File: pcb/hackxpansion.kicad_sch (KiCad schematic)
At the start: 1 part, among them J2 Conn_02x07_Counter_Clockwise

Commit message: STARTED WORKING ON SYMBOL
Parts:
- removed J2: Conn_02x07_Counter_Clockwise, Connector_PinSocket_2.54mm:PinSocket_2x07_P2.54mm_Horizontal, symbol Connector_Generic:Conn_02x07_Counter_Clockwise
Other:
- added sheet Module Bay 0 (module.kicad_sch)
- added sheet Module Bay 1 (module.kicad_sch)
- added sheet Module Bay 2 (module.kicad_sch)
- added sheet Module Bay 3 (module.kicad_sch)
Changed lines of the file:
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@@
 	(generator_version "10.0")
 	(paper "A4")
-	(symbol
-		(lib_id "Connector_Generic:Conn_02x07_Counter_Clockwise")
-		(at 242.57 87.63 0)
-		(unit 1)
-		(body_style 1)
-		(exclude_from_sim no)
-		(in_bom yes)
-		(on_board yes)
-		(in_pos_files yes)
-		(dnp no)
-		(fields_autoplaced yes)
-		(property "Reference" "J2"
-			(at 243.84 73.66 0)
-			(show_name no)
-			(do_not_autoplace no)
-			(effects
-				(font
-					(size 1.27 1.27)
-				)
-			)
-		)
-		(property "Value" "Conn_02x07_Counter_Clockwise"
-			(at 243.84 76.2 0)
-			(show_name no)
-			(do_not_autoplace no)
-			(effects
-				(font
-					(size 1.27 1.27)
-				)
-			)
-		)
-		(property "Footprint" "Connector_PinSocket_2.54mm:PinSocket_2x07_P2.54mm_Horizontal"
-			(at 242.57 87.63 0)
-			(hide yes)
-			(show_name no)
-			(do_not_autoplace no)
-			(effects
-				(font
-					(size 1.27 1.27)
-				)
-			)
-		)
-		(property "Datasheet" ""
-			(at 242.57 87.63 0)
-			(hide yes)
-			(show_name no)
-			(do_not_autoplace no)
-			(effects
-				(font
-					(size 1.27 1.27)
-				)
-			)
-		)
-		(property "Description" "Generic connector, double row, 02x07, counter clockwise pin numbering scheme (similar to DIP package numbering), script generated (kicad-library-utils/schlib/autogen/connector/)"
-			(at 242.57 87.63 0)
-			(hide yes)
-			(show_name no)
-			(do_not_autoplace no)
-			(effects
-				(font
-					(size 1.27 1.27)
-				)
-			)
-		)
-		(pin "4"
-		)
-		(pin "10"
-		)
-		(pin "1"
-		)
-		(pin "11"
-		)
-		(pin "3"
-		)
-		(pin "2"
-		)
-		(pin "7"
-		)
-		(pin "9"
-		)
-		(pin "12"
-		)
-		(pin "14"
-		)
-		(pin "5"
-		)
-		(pin "13"
-		)
-		(pin "8"
-		)
-		(pin "6"
-		)
-		(instances
-			(project "hackxpansion"
-				(path "/aaf5804d-3f78-442b-969e-39faa388db94"
-					(reference "J2")
-					(unit 1)
-				)
-			)
-		)
-	)
 	(sheet
 		(at 121.92 74.295)
@@
 	)
 	(sheet
-		(at 186.055 111.125)
+		(at 191.135 85.725)
 		(size 12.7 19.05)
 		(exclude_from_sim no)
@@
 		)
 		(property "Sheetname" "Display"
-			(at 186.055 110.4134 0)
+			(at 191.135 85.0134 0)
 			(show_name no)
 			(do_not_autoplace no)
@@
 		)
 		(property "Sheetfile" "disp.kicad_sch"
-			(at 186.055 130.7596 0)
+			(at 191.135 105.3596 0)
 			(show_name no)
 			(do_not_autoplace no)
@@
 				(path "/aaf5804d-3f78-442b-969e-39faa388db94"
 					(page "4")
+				)
+			)
+		)
+	)
+	(sheet
+		(at 232.41 133.35)
+		(size 12.7 11.43)
+		(exclude_from_sim no)
+		(in_bom yes)
+		(on_board yes)
+		(dnp no)
+		(fields_autoplaced yes)
+		(stroke
+			(width 0.1524)
+			(type solid)
+		)
+		(fill
+			(color 0 0 0 0)
+		)
+		(property "Sheetname" "Module Bay 0"
+			(at 232.41 132.6384 0)
+			(show_name no)
+			(do_not_autoplace no)
+			(effects
+				(font
+					(size 1.27 1.27)
+				)
+				(justify left bottom)
+			)
+		)
+		(property "Sheetfile" "module.kicad_sch"
+			(at 232.41 145.3646 0)
+			(show_name no)
+			(do_not_autoplace no)
+			(effects
+				(font
+					(size 1.27 1.27)
+				)
+				(justify left top)
+			)
+		)
+		(instances
+			(project "hackxpansion"
+				(path "/aaf5804d-3f78-442b-969e-39faa388db94"
+					(page "5")
+				)
+			)
+		)
+	)
+	(sheet
+		(at 257.81 133.35)
+		(size 12.7 11.43)
+		(exclude_from_sim no)
+		(in_bom yes)
+		(on_board yes)
+		(dnp no)
+		(fields_autoplaced yes)
+		(stroke
+			(width 0.1524)
+			(type solid)
+		)
+		(fill
+			(color 0 0 0 0)
+		)
+		(property "Sheetname" "Module Bay 1"
+			(at 257.81 132.6384 0)
+			(show_name no)
+			(do_not_autoplace no)
+			(effects
+				(font
+					(size 1.27 1.27)
+				)
+				(justify left bottom)
+			)
+		)
+		(property "Sheetfile" "module.kicad_sch"
+			(at 257.81 145.3646 0)
+			(show_name no)
+			(do_not_autoplace no)
+			(effects
+				(font
+					(size 1.27 1.27)
+				)
+				(justify left top)
+			)
+		)
+		(instances
+			(project "hackxpansion"
+				(path "/aaf5804d-3f78-442b-969e-39faa388db94"
+					(page "6")
+				)
+			)
+		)
+	)
+	(sheet
+		(at 257.81 152.4)
+		(size 12.7 11.43)
+		(exclude_from_sim no)
+		(in_bom yes)
+		(on_board yes)
+		(dnp no)
+		(fields_autoplaced yes)
+		(stroke
+			(width 0.1524)
+			(type solid)
+		)
+		(fill
+			(color 0 0 0 0)
+		)
+		(property "Sheetname" "Module Bay 3"
+			(at 257.81 151.6884 0)
+			(show_name no)
+			(do_not_autoplace no)
+			(effects
+				(font
+					(size 1.27 1.27)
+				)
+				(justify left bottom)
+			)
+		)
+		(property "Sheetfile" "module.kicad_sch"
+			(at 257.81 164.4146 0)
+			(show_name no)
+			(do_not_autoplace no)
+			(effects
+				(font
+					(size 1.27 1.27)
+				)
+				(justify left top)
+			)
+		)
+		(instances
+			(project "hackxpansion"
+				(path "/aaf5804d-3f78-442b-969e-39faa388db94"
+					(page "8")
 				)
 			)
@@
 				)
 			)
+		)
+	)
+	(sheet
+		(at 232.41 152.4)
+		(size 12.7 11.43)
+		(exclude_from_sim no)
+		(in_bom yes)
+		(on_board yes)
+		(dnp no)
+		(fields_autoplaced yes)
+		(stroke
+			(width 0.1524)
+			(type solid)
+		)
+		(fill
+			(color 0 0 0 0)
+		)
+		(property "Sheetname" "Module Bay 2"
+			(at 232.41 151.6884 0)
+			(show_name no)
+			(do_not_autoplace no)
+			(effects
+				(font
+					(size 1.27 1.27)
+				)
+				(justify left bottom)
+			)
+		)
+		(property "Sheetfile" "module.kicad_sch"
+			(at 232.41 164.4146 0)
+			(show_name no)
+			(do_not_autoplace no)
+			(effects
+				(font
+					(size 1.27 1.27)
+				)
+				(justify left top)
+			)
+		)
+		(instances
+			(project "hackxpansion"
+				(path "/aaf5804d-3f78-442b-969e-39faa388db94"
+					(page "7")
+				)
+			)

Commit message: worked on power
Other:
- added sheet Power (pwr.kicad_sch)
- sheet Display ports: added BACKLIGHT, CS, DC, RESET, spi{SPI}; removed none
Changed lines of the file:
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@@
 	)
 	(sheet
-		(at 191.135 85.725)
-		(size 12.7 19.05)
+		(at 197.485 85.725)
+		(size 12.7 15.875)
 		(exclude_from_sim no)
 		(in_bom yes)
@@
 		)
 		(property "Sheetname" "Display"
-			(at 191.135 85.0134 0)
+			(at 197.485 85.0134 0)
 			(show_name no)
 			(do_not_autoplace no)
@@
 		)
 		(property "Sheetfile" "disp.kicad_sch"
-			(at 191.135 105.3596 0)
-			(show_name no)
-			(do_not_autoplace no)
-			(effects
-				(font
-					(size 1.27 1.27)
-				)
-				(justify left top)
+			(at 197.485 102.1846 0)
+			(show_name no)
+			(do_not_autoplace no)
+			(effects
+				(font
+					(size 1.27 1.27)
+				)
+				(justify left top)
+			)
+		)
+		(pin "BACKLIGHT" input
+			(at 197.485 87.63 180)
+			(effects
+				(font
+					(size 1.27 1.27)
+				)
+				(justify left)
+			)
+		)
+		(pin "CS" input
+			(at 197.485 99.06 180)
+			(effects
+				(font
+					(size 1.27 1.27)
+				)
+				(justify left)
+			)
+		)
+		(pin "DC" input
+			(at 197.485 92.71 180)
+			(effects
+				(font
+					(size 1.27 1.27)
+				)
+				(justify left)
+			)
+		)
+		(pin "RESET" input
+			(at 197.485 90.17 180)
+			(effects
+				(font
+					(size 1.27 1.27)
+				)
+				(justify left)
+			)
+		)
+		(pin "spi{SPI}" input
+			(at 197.485 96.52 180)
+			(effects
+				(font
+					(size 1.27 1.27)
+				)
+				(justify left)
 			)
 		)
@@
 				(path "/aaf5804d-3f78-442b-969e-39faa388db94"
 					(page "4")
+				)
+			)
+		)
+	)
+	(sheet
+		(at 193.675 149.86)
+		(size 12.7 3.81)
+		(exclude_from_sim no)
+		(in_bom yes)
+		(on_board yes)
+		(dnp no)
+		(fields_autoplaced yes)
+		(stroke
+			(width 0.1524)
+			(type solid)
+		)
+		(fill
+			(color 0 0 0 0)
+		)
+		(property "Sheetname" "Power"
+			(at 193.675 149.1484 0)
+			(show_name no)
+			(do_not_autoplace no)
+			(effects
+				(font
+					(size 1.27 1.27)
+				)
+				(justify left bottom)
+			)
+		)
+		(property "Sheetfile" "pwr.kicad_sch"
+			(at 193.675 154.2546 0)
+			(show_name no)
+			(do_not_autoplace no)
+			(effects
+				(font
+					(size 1.27 1.27)
+				)
+				(justify left top)
+			)
+		)
+		(instances
+			(project "hackxpansion"
+				(path "/aaf5804d-3f78-442b-969e-39faa388db94"
+					(page "9")
 				)
 			)
@@
 	)
 	(sheet
-		(at 166.37 85.09)
-		(size 16.51 19.05)
+		(at 196.85 111.125)
+		(size 16.51 18.415)
 		(exclude_from_sim no)
 		(in_bom yes)
@@
 		)
 		(property "Sheetname" "ADC"
-			(at 166.37 84.3784 0)
+			(at 196.85 110.4134 0)
 			(show_name no)
 			(do_not_autoplace no)
@@
 		)
 		(property "Sheetfile" "ADC.kicad_sch"
-			(at 166.37 104.7246 0)
+			(at 196.85 130.1246 0)
 			(show_name no)
 			(do_not_autoplace no)
@@
 		)
 		(pin "ALERT" output
-			(at 166.37 87.63 180)
+			(at 196.85 113.03 180)
 			(effects
 				(font
@@
 		)
 		(pin "i2c0{I2C}" bidirectional
-			(at 166.37 90.17 180)
+			(at 196.85 115.57 180)
 			(effects
 				(font
@@
 		)
 		(pin "mod0{DET}" input
-			(at 182.88 93.98 0)
+			(at 213.36 119.38 0)
 			(effects
 				(font
@@
 		)
 		(pin "mod1{DET}" input
-			(at 182.88 96.52 0)
+			(at 213.36 121.92 0)
 			(effects
 				(font
@@
 		)
 		(pin "mod2{DET}" input
-			(at 182.88 99.06 0)
+			(at 213.36 124.46 0)
 			(effects
 				(font
@@
 		)
 		(pin "mod3{DET}" input
-			(at 182.88 101.6 0)
-			(effects
-				(font
+			(at 213.36 127 0)
+			(effects
+				(font

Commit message: worked on power
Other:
- note added: "E24 for the sensing resistors"
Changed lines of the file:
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@@
 	(generator_version "10.0")
 	(paper "A4")
+	(text "E24 for the sensing resistors"
+		(exclude_from_sim no)
+		(at 213.106 75.184 0)
+		(effects
+			(font
+				(size 1.27 1.27)
+			)
+		)
+	)
 	(sheet
 		(at 121.92 74.295)

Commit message: worked on power
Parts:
- added BT1: Battery_Cell, symbol Device:Battery_Cell
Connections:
- new net GND: BT1.2 (-)
- new net Power/+BATT: BT1.1 (+)
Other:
- added sheet USB (usb.kicad_sch)
- sheet Power ports: added +BATT, 3V3, VBUS; removed none
- sheet RP2354B ports: added USB_D+, USB_D-; removed none

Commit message: worked on io banks
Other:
- sheet ADC ports: added {I2C}; removed i2c0{I2C}
- sheet Module Bay 0 ports: added {DET}, {GPIO_BANK}; removed none
- sheet Module Bay 1 ports: added {DET}, {GPIO_BANK}; removed none
- sheet Module Bay 2 ports: added {DET}, {GPIO_BANK}; removed none
- sheet Module Bay 3 ports: added {DET}, {GPIO_BANK}; removed none
- sheet Power ports: added none; removed 3V3
- sheet RP2354B ports: added mod0{GPIO_BANK}, mod1{GPIO_BANK}, mod2{GPIO_BANK}, mod3{GPIO_BANK}, {USB}; removed USB_D+, USB_D-
- sheet USB ports: added VBUS, {USB}; removed none
- note removed: "E24 for the sensing resistors"
- moved on the sheet: BT1

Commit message: did a bunch of gpio bank stuff
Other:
- sheet Display ports: added {SPI}; removed spi{SPI}
- sheet RP2354B ports: added ADC_ALERT, DISP_BACKLIGHT, DISP_CS, DISP_DC, adc{I2C}, disp{SPI}; removed none
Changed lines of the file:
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@@
 	(wire
 		(pts
+			(xy 137.16 74.93) (xy 156.21 74.93)
+		)
+		(stroke
+			(width 0)
+			(type default)
+		)
+	)
+	(wire
+		(pts
+			(xy 137.16 69.85) (xy 156.21 69.85)
+		)
+		(stroke
+			(width 0)
+			(type default)
+		)
+	)
+	(wire
+		(pts
 			(xy 98.425 140.97) (xy 98.425 142.24)
 		)
@@
 		)
 	)
+	(bus
+		(pts
+			(xy 137.16 93.98) (xy 191.77 93.98)
+		)
+		(stroke
+			(width 0)
+			(type default)
+		)
+	)
 	(wire
 		(pts
@@
 		)
 	)
+	(wire
+		(pts
+			(xy 137.16 81.28) (xy 156.21 81.28)
+		)
+		(stroke
+			(width 0)
+			(type default)
+		)
+	)
 	(bus
 		(pts
@@
 	(bus
 		(pts
+			(xy 137.16 78.74) (xy 156.21 78.74)
+		)
+		(stroke
+			(width 0)
+			(type default)
+		)
+	)
+	(bus
+		(pts
 			(xy 92.71 123.19) (xy 92.71 114.3)
 		)
@@
 		(pts
 			(xy 140.97 114.3) (xy 140.97 144.78)
+		)
+		(stroke
+			(width 0)
+			(type default)
+		)
+	)
+	(wire
+		(pts
+			(xy 137.16 91.44) (xy 191.77 91.44)
 		)
 		(stroke
@@
 			)
 		)
+		(pin "ADC_ALERT" input
+			(at 137.16 91.44 0)
+			(effects
+				(font
+					(size 1.27 1.27)
+				)
+				(justify right)
+			)
+		)
+		(pin "adc{I2C}" bidirectional
+			(at 137.16 93.98 0)
+			(effects
+				(font
+					(size 1.27 1.27)
+				)
+				(justify right)
+			)
+		)
+		(pin "DISP_BACKLIGHT" output
+			(at 137.16 69.85 0)
+			(effects
+				(font
+					(size 1.27 1.27)
+				)
+				(justify right)
+			)
+		)
+		(pin "DISP_CS" output
+			(at 137.16 81.28 0)
+			(effects
+				(font
+					(size 1.27 1.27)
+				)
+				(justify right)
+			)
+		)
+		(pin "DISP_DC" output
+			(at 137.16 74.93 0)
+			(effects
+				(font
+					(size 1.27 1.27)
+				)
+				(justify right)
+			)
+		)
+		(pin "disp{SPI}" bidirectional
+			(at 137.16 78.74 0)
+			(effects
+				(font
+					(size 1.27 1.27)
+				)
+				(justify right)
+			)
+		)
 		(instances
 			(project "hackxpansion"
@@
 			)
 		)
-		(pin "spi{SPI}" input
+		(pin "{SPI}" bidirectional
 			(at 156.21 78.74 180)
 			(effects
@@
 		)
 		(pin "ALERT" output
-			(at 191.77 90.805 180)
-			(effects
-				(font
+			(at 191.77 91.44 180)
+			(effects
+				(font

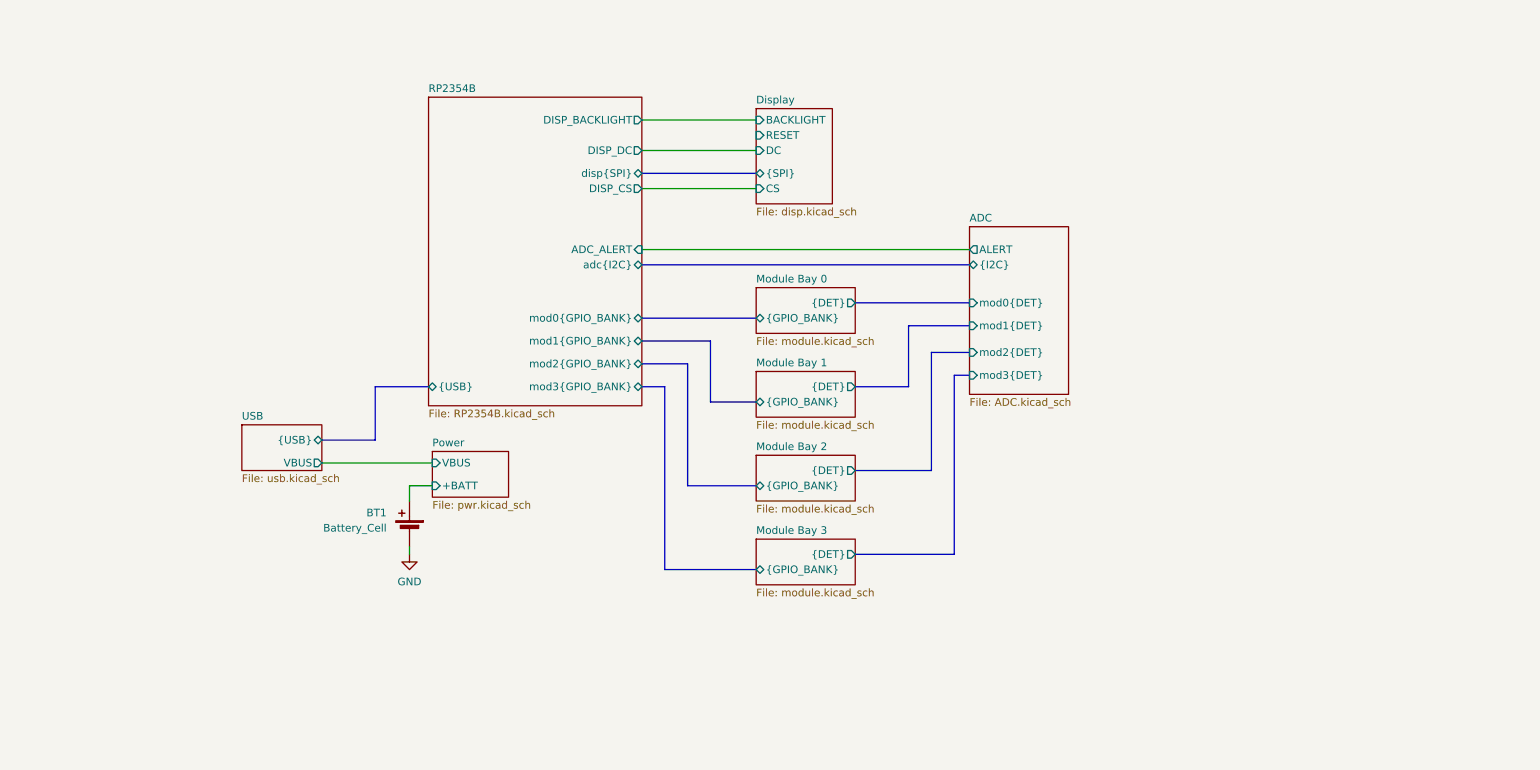
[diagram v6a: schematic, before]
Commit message: started to split up the schematic into two pcbs
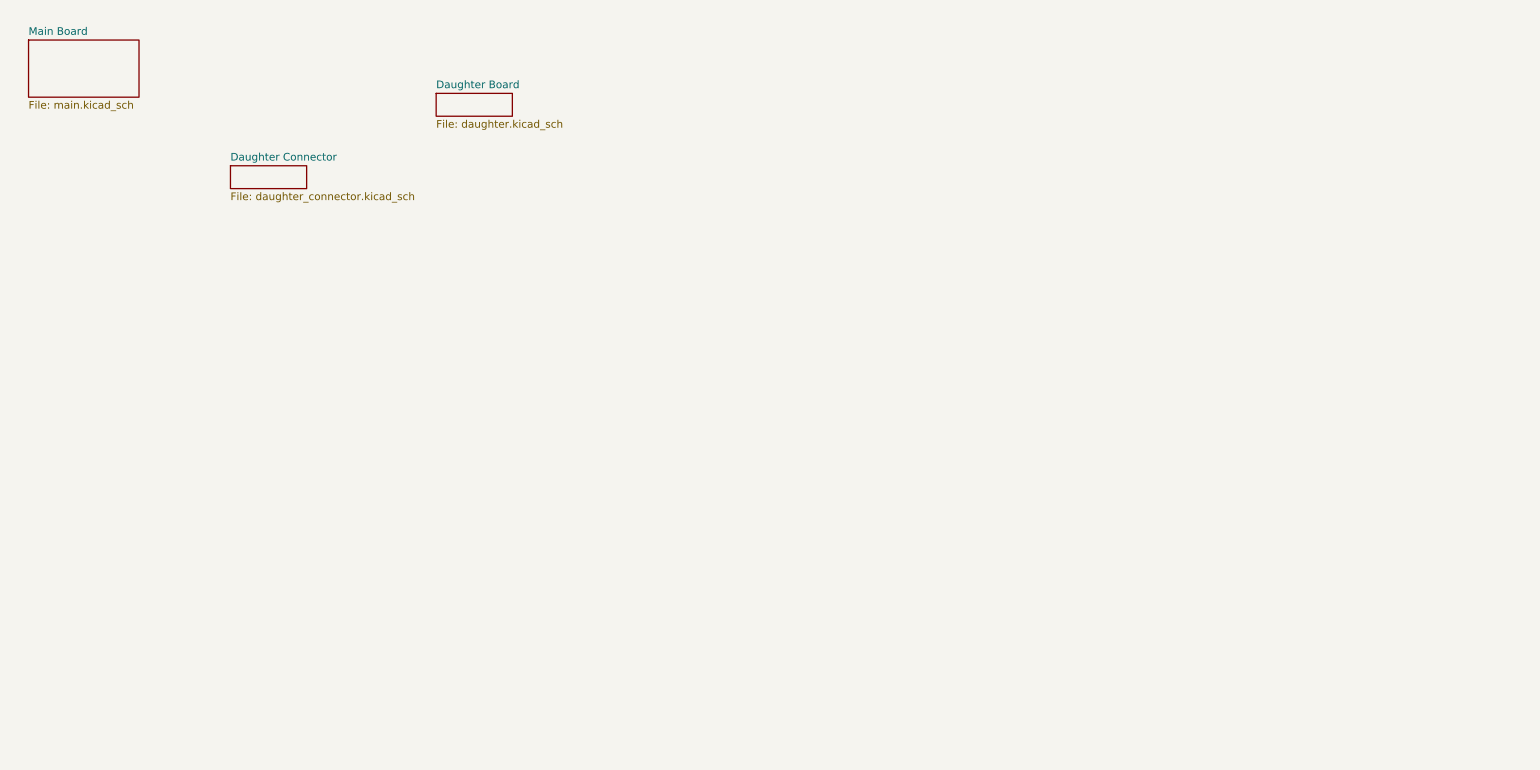
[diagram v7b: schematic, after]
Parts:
- removed BT1: Battery_Cell, symbol Device:Battery_Cell
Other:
- removed sheet ADC
- removed sheet Display
- removed sheet Module Bay 0
- removed sheet Module Bay 1
- removed sheet Module Bay 2
- removed sheet Module Bay 3
- removed sheet Power
- removed sheet RP2354B
- removed sheet USB
- added sheet Daughter Board (daughter.kicad_sch)
- added sheet Daughter Connector (daughter_connector.kicad_sch)
- added sheet Main Board (main.kicad_sch)

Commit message: moved stuff around
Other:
- sheet Daughter Connector renamed Daughter Connector Main
- added sheet Daughter Connector Daughter (daughter_conn.kicad_sch)
- sheet Daughter Board ports: added +3V3, GND, bank2{GPIO_BANK}, bank3{GPIO_BANK}, mod2{DET}, mod3{DET}; removed none
- sheet Daughter Connector Main: file daughter_connector.kicad_sch -> daughter_conn.kicad_sch
- sheet Daughter Connector Main ports: added +3V3, GND, bank2{GPIO_BANK}, bank3{GPIO_BANK}, mod2{DET}, mod3{DET}; removed none
- sheet Main Board ports: added +3V3, GND, bank2{GPIO_BANK}, bank3{GPIO_BANK}, mod2{DET}, mod3{DET}; removed none
